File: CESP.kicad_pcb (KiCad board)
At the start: 2 copper layers, 55.9 x 44.7 mm, 9 parts

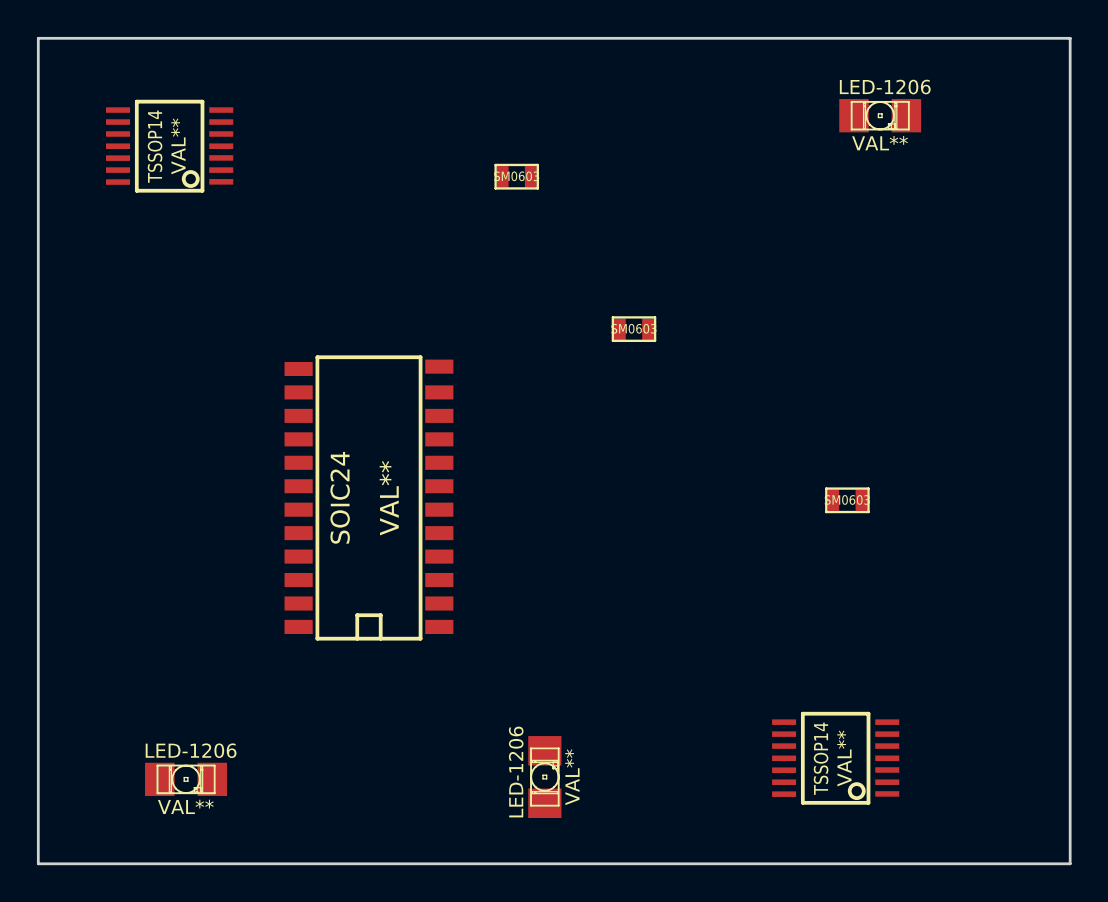
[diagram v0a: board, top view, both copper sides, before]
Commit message: Laid out a PCB with all required component types.
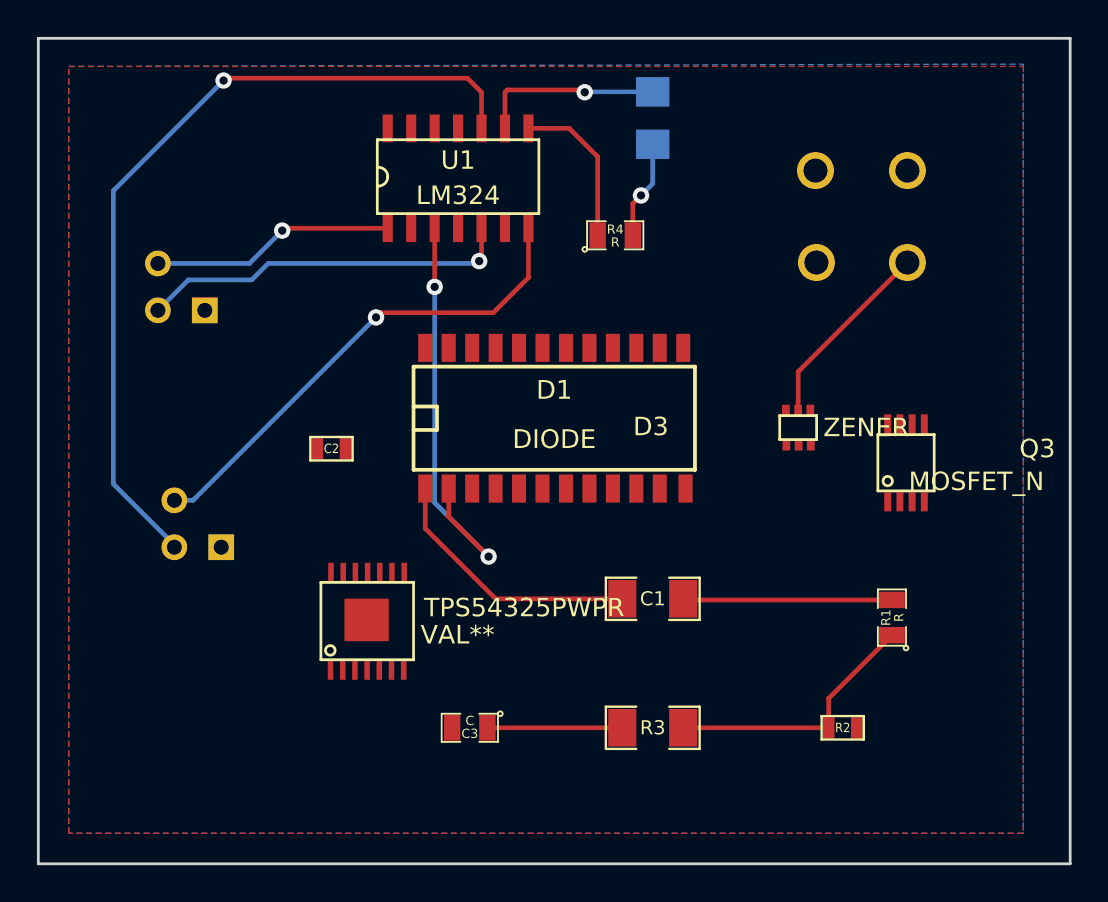
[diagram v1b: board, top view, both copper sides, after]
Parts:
- removed LED-1206 (x3): VAL**, LED-1206
- removed SM0603 (x3): Val**, SM0603
- removed SOIC24: VAL**, SOIC24
- removed TSSOP14 (x2): VAL**, TSSOP14
- added C1: C, SM1206, F.Cu at (189.2, 126.1)
- added C2: C, SM0603, F.Cu at (171.8, 118.0)
- added C3: C, SM0805, F.Cu at (179.3, 133.1)
- added D1: DIODE, SOIC24, F.Cu at (183.9, 116.3)
- added D2: LED, LED-1206, B.Cu at (189.2, 100.1)
- added D3: ZENER, BZX84C5V1S-7-F, F.Cu at (197.1, 116.8)
- added G***: LOGO, LOGO, B.Cu at (195.8, 126.6)
- added Q1: PN2222A, TO92, B.Cu at (163.7, 109.2)
- added Q2: PN2222A, TO92, B.Cu at (164.6, 122.0)
- added Q3: MOSFET_N, IRF7607TRPBF, F.Cu at (202.9, 118.7)
- added R1: R, SM0805, F.Cu at (202.2, 127.1)
- added R2: R, SM0603, F.Cu at (199.5, 133.1)
- added R3: R, SM1206, F.Cu at (189.2, 133.1)
- added R4: R, SM0805, F.Cu at (187.2, 106.4)
- added SW1: SW_PUSH, EG4791-ND, B.Cu at (200.5, 105.4)
- added TPS54325PWPR: VAL**, TPS54325PWPR, F.Cu at (173.7, 127.3)
- added U1: LM324, LM324DR, F.Cu at (178.7, 103.3)
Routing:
- net N-000003: track 0.00 -> 45.4 mm, vias 0 -> 1
- net N-000004: track 0.00 -> 26.8 mm, vias 0 -> 1
- net N-0000021: track 0.00 -> 23.6 mm, vias 0 -> 2
- net N-0000020: track 0.00 -> 20.3 mm, vias 0 -> 1
- net N-000009: track 0.00 -> 14.4 mm
- net VCC: track 0.00 -> 14.3 mm
- net N-0000022: track 0.00 -> 13.2 mm, vias 0 -> 1
- net N-000005: track 0.00 -> 11.3 mm
- net N-0000010: track 0.00 -> 10.5 mm
- net GND: track 0.00 -> 10.1 mm, vias 0 -> 1
- net N-0000016: track 0.00 -> 8.64 mm
- net N-000007: track 0.00 -> 7.30 mm
- net N-0000015: track 0.00 -> 5.38 mm, vias 0 -> 1
- added copper zone on B.Cu, net GND
- added copper zone on F.Cu, net VCC
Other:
- board text removed: "NOTE: THIS IS JUST A TEST BOARD REMOVE ALL COMPONENTS AND CREATE YOUR OWN INCLUDE SCHEMATIC HOOKUPS/NETLIST"
